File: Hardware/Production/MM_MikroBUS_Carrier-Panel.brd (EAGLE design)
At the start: 85.1 x 35.6 mm, 106 parts, among them J15 MICROMOD-2222-C, J2 QWIIC_RIGHT_ANGLE, J5 Vertical Qwiic Connector, J7 MIKROBUS_SMD_BLACK1, J9 CORTEX_JTAG_DEBUG_MINIMUM_PTH, U1 MCP73831, U2 AP7361C-33FGEUDFN-8

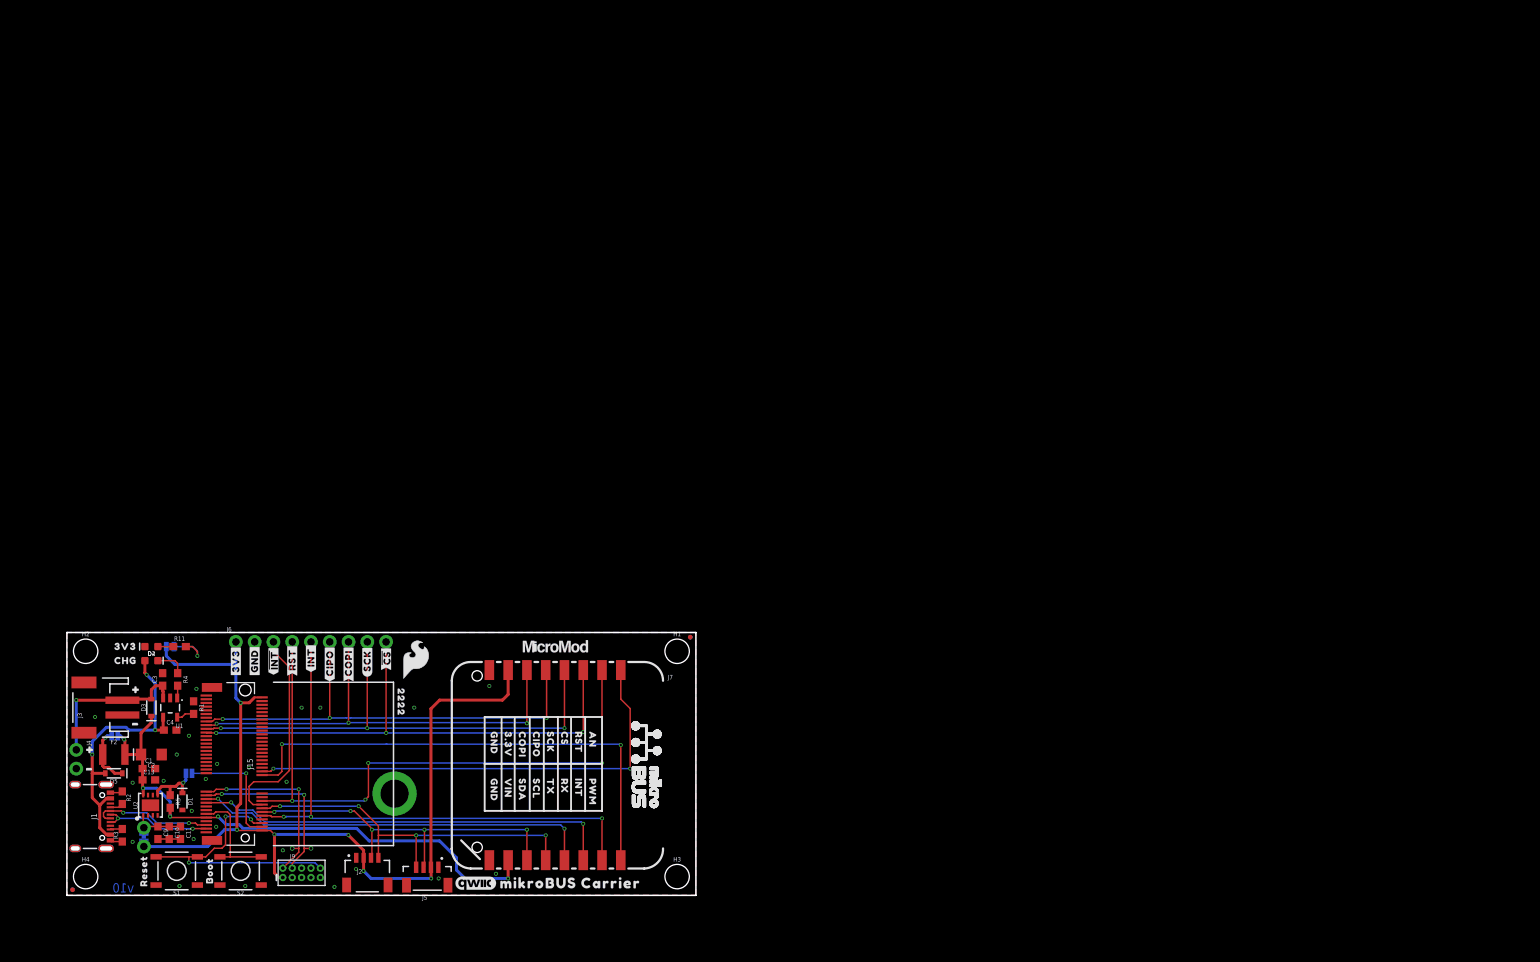
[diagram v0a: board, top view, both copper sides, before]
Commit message: Panelize and generate gerbers
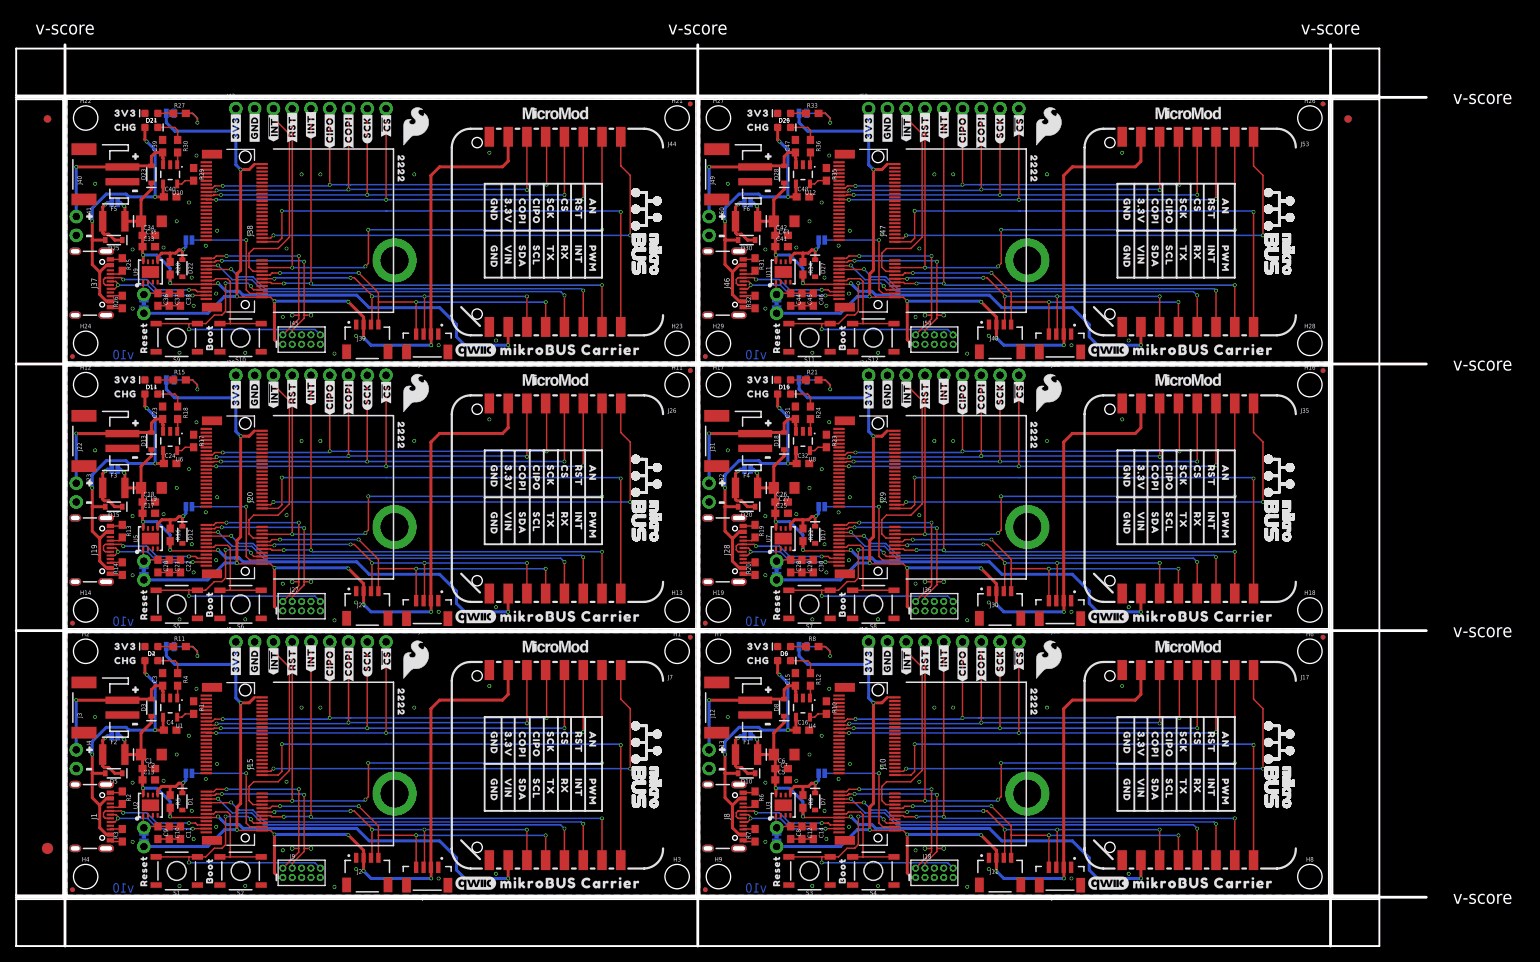
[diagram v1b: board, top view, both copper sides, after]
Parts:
- removed FRAME1: FRAME-LEDGER, SparkFun-Aesthetics:CREATIVE_COMMONS
- added BYP1, BYP2, BYP3, BYP4, BYP5: JUMPER-SMT_2_NO_SILK, SparkFun-Jumpers:SMT-JUMPER_2_NO_SILK
- added C12, C21, C29, C37, C45: 1.0uF, SparkFun-Capacitors:0603
- added C14, C17, C22, C25, C30, C33, C38, C41, C46, C5: 0.22uF, SparkFun-Capacitors:0603
- added C15, C16, C23, C24, C31, C32, C39, C40, C47, C48: 4.7uF, SparkFun-Capacitors:0603
- added C18, C26, C34, C42, C6: 0.1uF, SparkFun-Capacitors:0603
- added C19, C27, C35, C43, C7: 10uF, SparkFun-Capacitors:EIA3216
- added C20, C28, C36, C44, C8: 10uF, SparkFun-Capacitors:0603
- added D10, D13, D15, D18, D20, D23, D25, D28, D30, D8: 3A/10V/280mV, SparkFun-DiscreteSemi:SOD-323
- added D11, D16, D21, D26, D6: RED, SparkFun-LED:LED-0603
- added D12, D17, D22, D27, D7: 3.3V, SparkFun-DiscreteSemi:SOD-323
- added D14, D19, D24, D29, D9: Yellow, SparkFun-LED:LED-0603
- added E$1, E$2, E$3, E$4: (no value), SparkFun-Aesthetics:FIDUCIAL-1X2
- added E$5, E$6: (no value), SparkFun-Retired:FIDUCIAL-1.5X3
- added F1, F3, F4, F5, F6: 6V/2A, SparkFun-Fuses:1210
- added FD10, FD11, FD12, FD13, FD14, FD15, FD16, FD17, FD18, FD19, FD20, FD21, FD22, FD23, FD24, FD5, FD6, FD7, FD8, FD9: FIDUCIALUFIDUCIAL, SparkFun-Aesthetics:FIDUCIAL-MICRO
- added H10, H15, H20, H25, H30: STAND-OFF-REFLOW-M2.5_2.5MM_TALL, SparkFun-Hardware:STAND-OFF-REFLOW-M2.5
- added H11, H12, H13, H14, H16, H17, H18, H19, H21, H22, H23, H24, H26, H27, H28, H29, H6, H7, H8, H9: STAND-OFF, SparkFun-Hardware:STAND-OFF
- added J10, J20, J29, J38, J47: MICROMOD-2222-C, SparkFun-MicroMod:M.2-CONNECTOR-E
- added J11, J21, J30, J39, J48: QWIIC_RIGHT_ANGLE, SparkFun-Connectors:JST04_1MM_RA
- added J12, J22, J31, J40, J49: (no value), SparkFun-Connectors:JST-2-SMD
- added J13, J23, J32, J41, J50: (no value), SparkFun-Connectors:1X02_NO_SILK
- added J14, J24, J33, J42, J51: Vertical Qwiic Connector, SparkFun-Connectors:JST04_1MM_VERT
- added J16, J25, J34, J43, J52: (no value), SparkFun-Connectors:1X09_NO_SILK
- added J17, J26, J35, J44, J53: MIKROBUS_SMD_BLACK1, mikroBUS_SMD_BLACK:MIKROBUS_SMD_BLACK
- added J18, J27, J36, J45, J54: CORTEX_JTAG_DEBUG_MINIMUM_PTH, SparkFun-Connectors:2X5-PTH-1.27MM
- added J19, J28, J37, J46, J8: (no value), SparkFun-Connectors:USB-C-16P-2LAYER-PADS
- added JP1, JP11, JP3, JP7, JP9: 3V3 LED, SparkFun-Jumpers:SMT-JUMPER_2_NC_TRACE_SILK
- added JP10, JP12, JP2, JP5, JP8: VE, SparkFun-Jumpers:SMT-JUMPER_2_NO_SILK
- added LOGO10, LOGO13, LOGO16, LOGO4, LOGO7: QWIIC_LOGO_CONNECTOR, SparkFun-Aesthetics:QWIIC_5.5MM
- added LOGO11, LOGO14, LOGO17, LOGO5, LOGO8: OSHW-LOGOM, SparkFun-Aesthetics:OSHW-LOGO-M
- added LOGO12, LOGO15, LOGO18, LOGO6, LOGO9: SFE_LOGO_NAME_FLAME.2_INCH, SparkFun-Aesthetics:SFE_LOGO_NAME_FLAME_.2
- added MEAS1, MEAS2, MEAS3, MEAS4, MEAS5: JUMPER-COMBO_2_NC_TRACE, SparkFun-Jumpers:COMBO-JUMPER_2_NC_TRACE
- added R10, R17, R23, R29, R35: 2.2k, SparkFun-Resistors:0603
- added R12, R15, R18, R21, R24, R27, R30, R33, R36, R8: 1k, SparkFun-Resistors:0603
- added R13, R14, R19, R20, R25, R26, R31, R32, R6, R7: 5.1k, SparkFun-Resistors:0603
- added R16, R22, R28, R34, R9: 100k, SparkFun-Resistors:0603
- added S10, S12, S4, S6, S8: BOOT, SparkFun-Switches:TACTILE_SWITCH_SMD_5.2MM
- added S11, S3, S5, S7, S9: Reset, SparkFun-Switches:TACTILE_SWITCH_SMD_5.2MM
- added SWDCK1, SWDCK2, SWDCK3, SWDCK4, SWDCK5, SWDIO1, SWDIO2, SWDIO3, SWDIO4, SWDIO5: TEST-POINTTP_15TH_THRU, SparkFun-Connectors:TP_15TH
- added U$100, U$154, U$208, U$262, U$316: (no value), output:#3V3LED#0
- added U$101, U$155, U$209, U$263, U$317: MIKROBUS_LOGO, mikroBUS_SMD_BLACK:MIKROBUS_LOGO
- added U$102, U$156, U$210, U$264, U$318: (no value), output:#FUSEBYP#0
- added U$103, U$157, U$211, U$265, U$319: (no value), output:#3V3EN#0
- added U$104, U$158, U$212, U$266, U$320: (no value), output:#INT#0
- added U$105, U$106, U$159, U$160, U$213, U$214, U$267, U$268, U$321, U$322: (no value), output:#RST#0
- added U$107, U$161, U$215, U$269, U$323: (no value), output:#I2C_#INT##0
- added U$108, U$162, U$216, U$270, U$324: (no value), output:#MIK_INT#0
- added U$109, U$163, U$19, U$217, U$271: (no value), SparkFun-Aesthetics:SFE_LOGO_FLAME_.2
- added U$110, U$164, U$21, U$218, U$272: (no value), SparkFun-MicroMod:MICROMOD_LOGO_.5
- added U$111, U$165, U$219, U$273, U$56: (no value), output:CHG0
- added U$112, U$166, U$220, U$274, U$57: (no value), output:#MEAS#0
- added U$113, U$167, U$221, U$275, U$58: (no value), output:3V30
- added U$114, U$115, U$123, U$168, U$169, U$177, U$222, U$223, U$231, U$276, U$277, U$285, U$59, U$60, U$69: (no value), output:#GND#0
- added U$116, U$117, U$170, U$171, U$224, U$225, U$278, U$279, U$61, U$62: (no value), output:#CIPO#0
- added U$118, U$119, U$172, U$173, U$226, U$227, U$280, U$281, U$63, U$64: (no value), output:#COPI#0
- added U$120, U$121, U$174, U$175, U$228, U$229, U$282, U$283, U$65, U$66: (no value), output:#SCK#0
- added U$122, U$176, U$230, U$284, U$67: (no value), output:#VBAT#0
- added U$124, U$125, U$178, U$179, U$232, U$233, U$286, U$287, U$70, U$71: (no value), output:#0
- added U$126, U$127, U$180, U$181, U$234, U$235, U$288, U$289, U$72, U$73: (no value), buzzard_labels (1):#0
- added U$128, U$182, U$236, U$290, U$74: (no value), output:RESET0
- added U$129, U$183, U$237, U$291, U$75: (no value), output:BOOT0
- added U$130, U$184, U$238, U$292, U$76: (no value), output:22220
- added U$131, U$132, U$185, U$186, U$239, U$240, U$293, U$294, U$77, U$78: (no value), output:##CS##0
- added U$133, U$187, U$241, U$295, U$79: (no value), output:##INT##0
- added U$134, U$188, U$242, U$296, U$80: (no value), SparkFun-MicroMod:MICROMOD_LOGO_.35
- added U$135, U$136, U$189, U$190, U$243, U$244, U$297, U$298, U$81, U$82: (no value), output:#3V3#0
- added U$137, U$191, U$245, U$299, U$83: (no value), output:MIKROBUS_CARRIER0
- added U$138, U$192, U$246, U$300, U$84: (no value), output:AN0
- added U$139, U$193, U$247, U$301, U$85: (no value), output:RST0
- added U$140, U$194, U$248, U$302, U$86: (no value), output:CS0
- added U$141, U$195, U$249, U$303, U$87: (no value), output:SCK0
- added U$142, U$196, U$250, U$304, U$88: (no value), output:CIPO0
- added U$143, U$197, U$251, U$305, U$89: (no value), output:COPI0
- added U$144, U$198, U$252, U$306, U$90: (no value), output:3#3V0
- added U$145, U$146, U$199, U$200, U$253, U$254, U$307, U$308, U$91, U$92: (no value), output:GND0
- added U$147, U$201, U$255, U$309, U$93: (no value), output:PWM0
- added U$148, U$202, U$256, U$310, U$94: (no value), output:INT0
- added U$149, U$203, U$257, U$311, U$95: (no value), output:RX0
- added U$150, U$204, U$258, U$312, U$96: (no value), output:TX0
- added U$151, U$205, U$259, U$313, U$97: (no value), output:SCL0
- added U$152, U$206, U$260, U$314, U$98: (no value), output:SDA0
- added U$153, U$207, U$261, U$315, U$99: (no value), output:VIN0
- added U10, U12, U4, U6, U8: MCP73831, SparkFun-IC-Power:SOT23-5
- added U11, U3, U5, U7, U9: AP7361C-33FGEUDFN-8, SparkFun-IC-Power:UDFN-8
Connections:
- new net !BOOT!1: J10.11, S4.3, S4.4
- new net !BOOT!2: J20.11, S6.3, S6.4
- new net !BOOT!3: J29.11, S8.3, S8.4
- new net !BOOT!4: J38.11, S10.3, S10.4
- new net !BOOT!5: J47.11, S12.3, S12.4
- new net !RESET!1: J10.6, J18.10, S3.3, S3.4
- new net !RESET!2: J20.6, J27.10, S5.3, S5.4
- new net !RESET!3: J29.6, J36.10, S7.3, S7.4
- new net !RESET!4: J38.6, J45.10, S9.3, S9.4
- new net !RESET!5: J47.6, J54.10, S11.3, S11.4
- new net 3.3V1: J10.2, J10.74, J11.2, J14.2, J16.1, J17.7, J18.1, JP1.2, MEAS1.2, MEAS1.4
- new net 3.3V2: J20.2, J20.74, J21.2, J24.2, J25.1, J26.7, J27.1, JP3.2, MEAS2.2, MEAS2.4
- new net 3.3V3: J29.2, J29.74, J30.2, J33.2, J34.1, J35.7, J36.1, JP7.2, MEAS3.2, MEAS3.4
- new net 3.3V4: J38.2, J38.74, J39.2, J42.2, J43.1, J44.7, J45.1, JP9.2, MEAS4.2, MEAS4.4
- new net 3.3V5: J47.2, J47.74, J48.2, J51.2, J52.1, J53.7, J54.1, JP11.2, MEAS5.2, MEAS5.4
- new net 3.3V_EN1: J10.4, JP2.1
- new net 3.3V_EN2: J20.4, JP5.1
- new net 3.3V_EN3: J29.4, JP8.1
- new net 3.3V_EN4: J38.4, JP10.1
- new net 3.3V_EN5: J47.4, JP12.1
- new net AN1: J10.34, J17.1
- new net AN2: J20.34, J26.1
- new net AN3: J29.34, J35.1
- new net AN4: J38.34, J44.1
- new net AN5: J47.34, J53.1
- new net GND1: C12.2, C14.2, C15.2, C16.2, C5.2, C6.2, C7.-, C8.2, D6.C, D7.A, H10.1, J10.1, J10.33, J10.36, J10.39, J10.45, J10.7, J10.75, J11.1, J12.1, J13.2, J14.1, J16.2, J17.8, J17.9, J18.3, J18.5, J18.9, J8.GND, J8.GND2, R10.1, R6.1, R7.1, S3.1, S3.2, S4.1, S4.2, U3.4, U3.EP, U4.2
- new net GND2: C17.2, C18.2, C19.-, C20.2, C21.2, C22.2, C23.2, C24.2, D11.C, D12.A, H15.1, J19.GND, J19.GND2, J20.1, J20.33, J20.36, J20.39, J20.45, J20.7, J20.75, J21.1, J22.1, J23.2, J24.1, J25.2, J26.8, J26.9, J27.3, J27.5, J27.9, R13.1, R14.1, R17.1, S5.1, S5.2, S6.1, S6.2, U5.4, U5.EP, U6.2
- new net GND3: C25.2, C26.2, C27.-, C28.2, C29.2, C30.2, C31.2, C32.2, D16.C, D17.A, H20.1, J28.GND, J28.GND2, J29.1, J29.33, J29.36, J29.39, J29.45, J29.7, J29.75, J30.1, J31.1, J32.2, J33.1, J34.2, J35.8, J35.9, J36.3, J36.5, J36.9, R19.1, R20.1, R23.1, S7.1, S7.2, S8.1, S8.2, U7.4, U7.EP, U8.2
- new net GND4: C33.2, C34.2, C35.-, C36.2, C37.2, C38.2, C39.2, C40.2, D21.C, D22.A, H25.1, J37.GND, J37.GND2, J38.1, J38.33, J38.36, J38.39, J38.45, J38.7, J38.75, J39.1, J40.1, J41.2, J42.1, J43.2, J44.8, J44.9, J45.3, J45.5, J45.9, R25.1, R26.1, R29.1, S10.1, S10.2, S9.1, S9.2, U10.2, U9.4, U9.EP
- new net GND5: C41.2, C42.2, C43.-, C44.2, C45.2, C46.2, C47.2, C48.2, D26.C, D27.A, H30.1, J46.GND, J46.GND2, J47.1, J47.33, J47.36, J47.39, J47.45, J47.7, J47.75, J48.1, J49.1, J50.2, J51.1, J52.2, J53.8, J53.9, J54.3, J54.5, J54.9, R31.1, R32.1, R35.1, S11.1, S11.2, S12.1, S12.2, U11.4, U11.EP, U12.2
- new net I2C_!INT!1: J10.16, J16.3
- new net I2C_!INT!2: J20.16, J25.3
- new net I2C_!INT!3: J29.16, J34.3
- new net I2C_!INT!4: J38.16, J43.3
- new net I2C_!INT!5: J47.16, J52.3
- new net MIK_INT1: J10.10, J16.5, J17.15
- new net MIK_INT2: J20.10, J25.5, J26.15
- new net MIK_INT3: J29.10, J34.5, J35.15
- new net MIK_INT4: J38.10, J43.5, J44.15
- new net MIK_INT5: J47.10, J52.5, J53.15
- new net MIK_RST1: J10.18, J16.4, J17.2
- new net MIK_RST2: J20.18, J25.4, J26.2
- new net MIK_RST3: J29.18, J34.4, J35.2
- new net MIK_RST4: J38.18, J43.4, J44.2
- new net MIK_RST5: J47.18, J52.4, J53.2
- new net N$12: D6.A, R8.1
- new net N$13: C12.1, C14.1, C8.1, MEAS1.1, MEAS1.3, U3.1
- new net N$14: R10.2, U4.5
- new net N$15: D9.C, R12.1
- new net N$16: R12.2, U4.1
- new net N$17: J19.A5, R13.2
- new net N$18: J19.B5, R14.2
- new net N$19: JP3.1, R15.2
- new net N$20: D11.A, R15.1
- new net N$21: C20.1, C21.1, C22.1, MEAS2.1, MEAS2.3, U5.1
- new net N$22: R17.2, U6.5
- new net N$23: D14.C, R18.1
- new net N$24: R18.2, U6.1
- new net N$25: J28.A5, R19.2
- new net N$26: J28.B5, R20.2
- new net N$27: JP7.1, R21.2
- new net N$28: D16.A, R21.1
- new net N$29: C28.1, C29.1, C30.1, MEAS3.1, MEAS3.3, U7.1
- new net N$30: R23.2, U8.5
- new net N$31: D19.C, R24.1
- new net N$32: R24.2, U8.1
- new net N$33: J37.A5, R25.2
- new net N$34: J37.B5, R26.2
- new net N$35: JP9.1, R27.2
- new net N$36: D21.A, R27.1
- new net N$37: C36.1, C37.1, C38.1, MEAS4.1, MEAS4.3, U9.1
- new net N$38: R29.2, U10.5
- new net N$39: D24.C, R30.1
- new net N$40: R30.2, U10.1
- new net N$41: J46.A5, R31.2
- new net N$42: J46.B5, R32.2
- new net N$43: JP11.1, R33.2
- new net N$44: D26.A, R33.1
- new net N$45: C44.1, C45.1, C46.1, MEAS5.1, MEAS5.3, U11.1
- new net N$46: R35.2, U12.5
- new net N$47: D29.C, R36.1
- new net N$48: R36.2, U12.1
- new net N$5: J8.A5, R6.2
- new net N$7: J8.B5, R7.2
- new net N$9: JP1.1, R8.2
- new net PWM1: J10.32, J17.16
- new net PWM2: J20.32, J26.16
- new net PWM3: J29.32, J35.16
- new net PWM4: J38.32, J44.16
- new net PWM5: J47.32, J53.16
- new net RX1: J10.17, J17.14
- new net RX2: J20.17, J26.14
- new net RX3: J29.17, J35.14
- new net RX4: J38.17, J44.14
- new net RX5: J47.17, J53.14
- new net SCL1: J10.14, J11.4, J14.4, J17.12
- new net SCL2: J20.14, J21.4, J24.4, J26.12
- new net SCL3: J29.14, J30.4, J33.4, J35.12
- new net SCL4: J38.14, J39.4, J42.4, J44.12
- new net SCL5: J47.14, J48.4, J51.4, J53.12
- new net SDA1: J10.12, J11.3, J14.3, J17.11
- new net SDA2: J20.12, J21.3, J24.3, J26.11
- new net SDA3: J29.12, J30.3, J33.3, J35.11
- new net SDA4: J38.12, J39.3, J42.3, J44.11
- new net SDA5: J47.12, J48.3, J51.3, J53.11
- new net SPI_!CS!1: J10.55, J16.9, J17.3
- new net SPI_!CS!2: J20.55, J25.9, J26.3
- new net SPI_!CS!3: J29.55, J34.9, J35.3
- new net SPI_!CS!4: J38.55, J43.9, J44.3
- new net SPI_!CS!5: J47.55, J52.9, J53.3
- new net SPI_CIPO1: J10.61, J16.6, J17.5
- new net SPI_CIPO2: J20.61, J25.6, J26.5
- new net SPI_CIPO3: J29.61, J34.6, J35.5
- new net SPI_CIPO4: J38.61, J43.6, J44.5
- new net SPI_CIPO5: J47.61, J52.6, J53.5
- new net SPI_COPI1: J10.59, J16.7, J17.6
- new net SPI_COPI2: J20.59, J25.7, J26.6
- new net SPI_COPI3: J29.59, J34.7, J35.6
- new net SPI_COPI4: J38.59, J43.7, J44.6
- new net SPI_COPI5: J47.59, J52.7, J53.6
- new net SPI_SCK1: J10.57, J16.8, J17.4
- new net SPI_SCK2: J20.57, J25.8, J26.4
- new net SPI_SCK3: J29.57, J34.8, J35.4
- new net SPI_SCK4: J38.57, J43.8, J44.4
- new net SPI_SCK5: J47.57, J52.8, J53.4
- new net SWDCK1: J10.21, J18.4, SWDCK1.1
- new net SWDCK2: J20.21, J27.4, SWDCK2.1
- new net SWDCK3: J29.21, J36.4, SWDCK3.1
- new net SWDCK4: J38.21, J45.4, SWDCK4.1
- new net SWDCK5: J47.21, J54.4, SWDCK5.1
- new net SWDIO1: J10.23, J18.2, SWDIO1.1
- new net SWDIO2: J20.23, J27.2, SWDIO2.1
- new net SWDIO3: J29.23, J36.2, SWDIO3.1
- new net SWDIO4: J38.23, J45.2, SWDIO4.1
- new net SWDIO5: J47.23, J54.2, SWDIO5.1
- new net TX1: J10.19, J17.13
- new net TX2: J20.19, J26.13
- new net TX3: J29.19, J35.13
- new net TX4: J38.19, J44.13
- new net TX5: J47.19, J53.13
- new net USB_D+1: J10.3, J8.A6, J8.B6
- new net USB_D+2: J19.A6, J19.B6, J20.3
- new net USB_D+3: J28.A6, J28.B6, J29.3
- new net USB_D+4: J37.A6, J37.B6, J38.3
- new net USB_D+5: J46.A6, J46.B6, J47.3
- new net USB_D-1: J10.5, J8.A7, J8.B7
- new net USB_D-2: J19.A7, J19.B7, J20.5
- new net USB_D-3: J28.A7, J28.B7, J29.5
- new net USB_D-4: J37.A7, J37.B7, J38.5
- new net USB_D-5: J46.A7, J46.B7, J47.5
- new net VIN1: BYP1.2, C5.1, C6.1, C7.+, D8.C, F1.2, J10.9, J17.10, R9.2, U3.8
- new net VIN2: BYP2.2, C17.1, C18.1, C19.+, D13.C, F3.2, J20.9, J26.10, R16.2, U5.8
- new net VIN3: BYP3.2, C25.1, C26.1, C27.+, D18.C, F4.2, J29.9, J35.10, R22.2, U7.8
- new net VIN4: BYP4.2, C33.1, C34.1, C35.+, D23.C, F5.2, J38.9, J44.10, R28.2, U9.8
- new net VIN5: BYP5.2, C41.1, C42.1, C43.+, D28.C, F6.2, J47.9, J53.10, R34.2, U11.8
- new net VREG_EN1: D7.C, JP2.2, R9.1, U3.5
- new net VREG_EN2: D12.C, JP5.2, R16.1, U5.5
- new net VREG_EN3: D17.C, JP8.2, R22.1, U7.5
- new net VREG_EN4: D22.C, JP10.2, R28.1, U9.5
- new net VREG_EN5: D27.C, JP12.2, R34.1, U11.5
- new net V_BATT1: C15.1, D8.A, J12.2, J13.1, U4.3
- new net V_BATT2: C23.1, D13.A, J22.2, J23.1, U6.3
- new net V_BATT3: C31.1, D18.A, J31.2, J32.1, U8.3
- new net V_BATT4: C39.1, D23.A, J40.2, J41.1, U10.3
- new net V_BATT5: C47.1, D28.A, J49.2, J50.1, U12.3
- new net V_USB1: C16.1, D10.A, D9.A, J8.VBUS1, J8.VBUS2, U4.4
- new net V_USB2: C24.1, D14.A, D15.A, J19.VBUS1, J19.VBUS2, U6.4
- new net V_USB3: C32.1, D19.A, D20.A, J28.VBUS1, J28.VBUS2, U8.4
- new net V_USB4: C40.1, D24.A, D25.A, J37.VBUS1, J37.VBUS2, U10.4
- new net V_USB5: C48.1, D29.A, D30.A, J46.VBUS1, J46.VBUS2, U12.4
- new net V_USB_1: BYP1.1, D10.C, F1.1
- new net V_USB_3: BYP2.1, D15.C, F3.1
- new net V_USB_4: BYP3.1, D20.C, F4.1
- new net V_USB_5: BYP4.1, D25.C, F5.1
- new net V_USB_6: BYP5.1, D30.C, F6.1
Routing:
- net 3.3V2: track 0.00 -> 129.3 mm, vias 0 -> 6
- net 3.3V1: track 0.00 -> 129.3 mm, vias 0 -> 6
- net 3.3V5: track 0.00 -> 129.3 mm, vias 0 -> 6
- net 3.3V4: track 0.00 -> 129.3 mm, vias 0 -> 6
- net 3.3V3: track 0.00 -> 129.3 mm, vias 0 -> 6
- net MIK_RST3: track 0.00 -> 84.9 mm, vias 0 -> 4
- net MIK_RST5: track 0.00 -> 84.9 mm, vias 0 -> 4
- net MIK_RST4: track 0.00 -> 84.9 mm, vias 0 -> 4
- net MIK_RST2: track 0.00 -> 84.9 mm, vias 0 -> 4
- net MIK_RST1: track 0.00 -> 84.9 mm, vias 0 -> 4
- net VIN5: track 0.00 -> 77.1 mm, vias 0 -> 5
- net VIN3: track 0.00 -> 77.1 mm, vias 0 -> 5
- net VIN1: track 0.00 -> 77.1 mm, vias 0 -> 5
- net VIN2: track 0.00 -> 77.1 mm, vias 0 -> 5
- net VIN4: track 0.00 -> 77.1 mm, vias 0 -> 5
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- added copper zone on layer 1, net GND1
- added copper zone on layer 16, net GND1
- added copper zone on layer 1, net GND2
- added copper zone on layer 16, net GND2
- added copper zone on layer 1, net GND3
- added copper zone on layer 16, net GND3
- added copper zone on layer 1, net GND4
- added copper zone on layer 16, net GND4
- added copper zone on layer 1, net GND5
- added copper zone on layer 16, net GND5
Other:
- board size 85.1 x 35.6 mm -> 190.8 x 121.9 mm
- board text added: "v-score"
- board text removed: "All units in inches."
- board text removed: "Priyanka Makin"

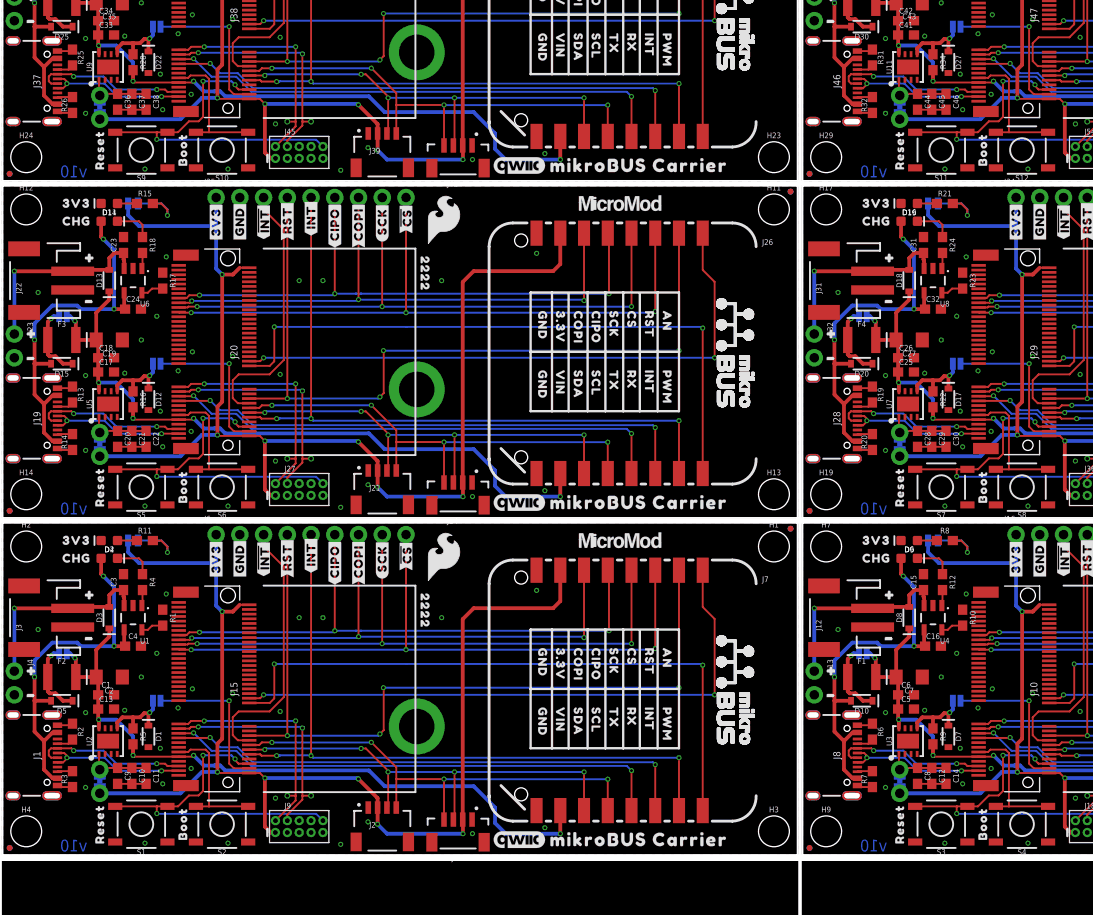
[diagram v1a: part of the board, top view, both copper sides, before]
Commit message: Re-panelize and generate new gerbers for v11
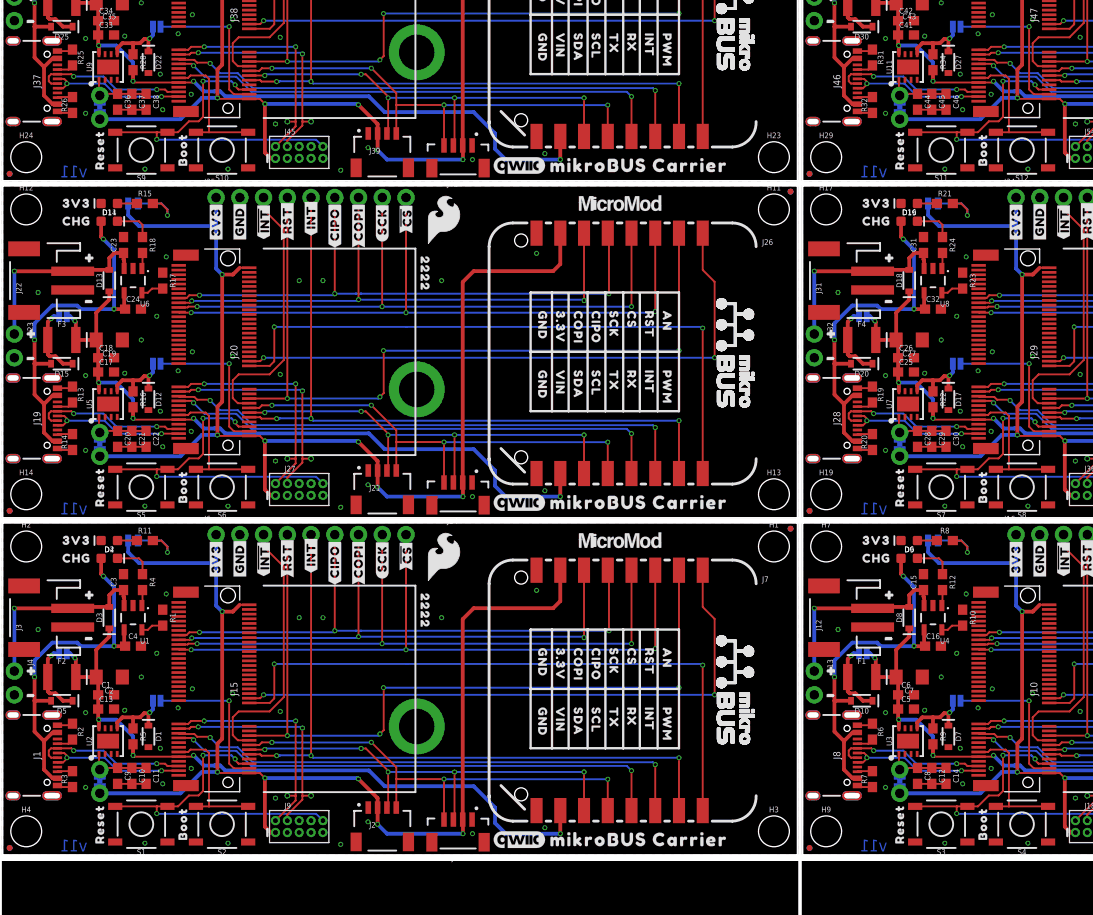
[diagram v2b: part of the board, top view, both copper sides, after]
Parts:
- U$106, U$160, U$214, U$268, U$322: device output:#RST#0 -> output:#I2C_#INT##0
- U$107, U$161, U$215, U$269, U$323: device output:#I2C_#INT##0 -> output:#MIK_INT#0
- U$108, U$162, U$216, U$270, U$324: device output:#MIK_INT#0 -> output:#MIK_RST#0
- U$18: device output:#RST#0 -> SparkFun-Aesthetics:SFE_LOGO_FLAME_.2
- U$19: device SparkFun-Aesthetics:SFE_LOGO_FLAME_.2 -> output:#MIK_RST#0
- moved U$19 102.5 mm to (30.5, 26.8), flipped to the bottom, turned to 90 degrees
- moved U$18 102.4 mm to (132.8, 31.9), flipped to the top, turned to 0 degrees
- moved U$161 5.08 mm to (33.0, 63.1)
- moved U$269 5.08 mm to (33.0, 99.2)
- moved U$107 5.08 mm to (118.6, 27.1)
- moved U$215 5.08 mm to (118.6, 63.1)
- moved U$323 5.08 mm to (118.6, 99.2)
- moved U$322 3.59 mm to (113.5, 99.3)
- moved U$106 3.59 mm to (113.5, 27.2)
- moved U$214 3.59 mm to (113.5, 63.2)
- moved U$268 3.59 mm to (27.9, 99.3)
- moved U$160 3.59 mm to (27.9, 63.2)
- moved U$162 2.55 mm to (30.5, 62.9)
- moved U$270 2.55 mm to (30.5, 98.9)
- moved U$108 2.55 mm to (116.1, 26.8)
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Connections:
- net RX: now also J15.19; no longer J15.17
- net RX1: now also J10.19; no longer J10.17
- net RX2: now also J20.19; no longer J20.17
- net RX3: now also J29.19; no longer J29.17
- net RX4: now also J38.19; no longer J38.17
- net RX5: now also J47.19; no longer J47.17
- net TX: now also J15.17; no longer J15.19
- net TX1: now also J10.17; no longer J10.19
- net TX2: now also J20.17; no longer J20.19
- net TX3: now also J29.17; no longer J29.19
- net TX4: now also J38.17; no longer J38.19
- net TX5: now also J47.17; no longer J47.19
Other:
- board text added: "v11"
- board text removed: "v10"
